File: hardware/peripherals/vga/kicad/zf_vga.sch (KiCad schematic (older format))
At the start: 34 parts, among them J1 Conn_02x04_Odd_Even, J2 Conn_02x13_Odd_Even, J3 DB15_Female, J4 DB9_Male, J5 DB9_Male, SW1 SW_DIP_x03, U1 4040, U10 74HC165, U11 AS6C6264, U12 74HC541, U13 74HC541, U14 74HC541, U2 4040, U3 GAL16V8, U4 GAL16V8, U5 74HC541, U6 74HC541, U7 74HC00, U8 74HC04, U9 74HC74, X1 CXO_DIP14

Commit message: Started PCB
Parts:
- removed J1: Conn_02x04_Odd_Even, symbol Connector_Generic:Conn_02x04_Odd_Even
- C1, C2, C3, C4, C5: footprint (none) -> Capacitor_THT:C_Disc_D7.5mm_W2.5mm_P5.00mm
- J2: footprint (none) -> Connector_IDC:IDC-Header_2x13_P2.54mm_Vertical
- R1, R2, R3, R4, R5, R6, R7, R8: footprint (none) -> Resistor_THT:R_Axial_DIN0207_L6.3mm_D2.5mm_P7.62mm_Horizontal
- SW1: footprint (none) -> Button_Switch_THT:SW_DIP_SPSTx03_Slide_6.7x9.18mm_W7.62mm_P2.54mm_LowProfile
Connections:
- no-connect marks 35 -> 29
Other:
- moved on the sheet: U12

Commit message: Bypass caps
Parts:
- added C10, C11, C12, C13, C14, C15, C16, C17, C18, C19, C20, C6, C7, C8, C9: 0.1uF, Capacitor_THT:C_Disc_D7.5mm_W2.5mm_P5.00mm, symbol Device:C_Small
- SW1: footprint Button_Switch_THT:SW_DIP_SPSTx03_Slide_6.7x9.18mm_W7.62mm_P2.54mm_LowProfile -> Package_DIP:DIP-6_W7.62mm_LongPads
- U1, U10, U2: footprint Package_DIP:DIP-16_W7.62mm -> Package_DIP:DIP-16_W7.62mm_LongPads
- U11: footprint Package_DIP:DIP-28_W15.24mm -> Package_DIP:DIP-28_W15.24mm_LongPads
- U12, U13, U14, U3, U4, U5, U6: footprint Package_DIP:DIP-20_W7.62mm -> Package_DIP:DIP-20_W7.62mm_LongPads
- X1: footprint Oscillator:Oscillator_DIP-14 -> Oscillator:Oscillator_DIP-14_LargePads
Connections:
- net A0: now also U13.11 (Y7), U5.15 (Y3); no longer U13.18 (Y0), U5.18 (Y0)
- net A1: now also U13.12 (Y6), U5.16 (Y2); no longer U13.17 (Y1), U5.17 (Y1)
- net A10: now also U14.18 (Y0), U6.18 (Y0); no longer U14.16 (Y2), U6.12 (Y6)
- net A2: now also U13.13 (Y5), U5.17 (Y1); no longer U13.16 (Y2), U5.16 (Y2)
- net A3: now also U13.14 (Y4), U5.18 (Y0); no longer U13.15 (Y3), U5.15 (Y3)
- net A4: now also U13.15 (Y3), U6.12 (Y6); no longer U13.14 (Y4), U6.18 (Y0)
- net A5: now also U13.16 (Y2), U6.13 (Y5); no longer U13.13 (Y5), U6.17 (Y1)
- net A6: now also U13.17 (Y1), U6.14 (Y4); no longer U13.12 (Y6), U6.16 (Y2)
- net A7: now also U13.18 (Y0); no longer U13.11 (Y7)
- net A8: now also U14.16 (Y2), U6.16 (Y2); no longer U14.18 (Y0), U6.14 (Y4)
- net A9: now also U6.17 (Y1); no longer U6.13 (Y5)
- net D0: now also U12.11 (Y7); no longer U12.18 (Y0)
- net D1: now also U12.12 (Y6); no longer U12.17 (Y1)
- net D2: now also U12.13 (Y5); no longer U12.16 (Y2)
- net D3: now also U12.14 (Y4); no longer U12.15 (Y3)
- net D4: now also U12.15 (Y3); no longer U12.14 (Y4)
- net D5: now also U12.16 (Y2); no longer U12.13 (Y5)
- net D6: now also U12.17 (Y1); no longer U12.12 (Y6)
- net D7: now also U12.18 (Y0); no longer U12.11 (Y7)
- net GND: now also C4.2, C5.2, C10.2, C11.2, C12.2, C13.2, C14.2, C15.2, C16.2, C17.2, C18.2, C19.2, C20.2, C6.2, C7.2, C8.2, C9.2; no longer C4.1, C5.1
- net L0: now also U4.11 (I10/~OE~); no longer U4.1 (I1/CLK)
- net L1: now also U4.9 (I9); no longer U4.2 (I2)
- net L2: now also U4.8 (I8), U6.8 (A6); no longer U4.3 (I3), U6.2 (A0)
- net L3: now also U4.7 (I7), U6.7 (A5); no longer U4.4 (I4), U6.3 (A1)
- net L4: now also U4.6 (I6), U6.6 (A4); no longer U4.5 (I5), U6.4 (A2)
- net L5: now also U4.5 (I5); no longer U4.6 (I6)
- net L6: now also U4.4 (I4), U6.4 (A2); no longer U4.7 (I7), U6.6 (A4)
- net L7: now also U4.3 (I3), U6.3 (A1); no longer U4.8 (I8), U6.7 (A5)
- net L8: now also U4.2 (I2), U6.2 (A0); no longer U4.9 (I9), U6.8 (A6)
- net L9: now also U4.1 (I1/CLK); no longer U4.11 (I10/~OE~)
- net P0: now also U3.11 (I10/~OE~); no longer U3.1 (I1/CLK)
- net P1: now also U3.9 (I9); no longer U3.2 (I2)
- net P2: now also U3.8 (I8); no longer U3.3 (I3)
- net P3: now also U3.7 (I7); no longer U3.4 (I4)
- net P4: now also U3.6 (I6); no longer U3.5 (I5)
- net P5: now also U3.5 (I5), U5.5 (A3); no longer U3.6 (I6), U5.2 (A0)
- net P6: now also U3.4 (I4), U5.4 (A2); no longer U3.7 (I7), U5.3 (A1)
- net P7: now also U3.3 (I3), U5.3 (A1); no longer U3.8 (I8), U5.4 (A2)
- net P8: now also U3.2 (I2), U5.2 (A0); no longer U3.9 (I9), U5.5 (A3)
- net P9: now also U3.1 (I1/CLK); no longer U3.11 (I10/~OE~)
- net PA0: now also U12.9 (A7); no longer U12.2 (A0)
- net PA1: now also U12.8 (A6); no longer U12.3 (A1)
- net PA2: now also U12.7 (A5); no longer U12.4 (A2)
- net PA3: now also U12.6 (A4); no longer U12.5 (A3)
- net PA4: now also U12.5 (A3); no longer U12.6 (A4)
- net PA5: now also U12.4 (A2); no longer U12.7 (A5)
- net PA6: now also U12.3 (A1); no longer U12.8 (A6)
- net PA7: now also U12.2 (A0); no longer U12.9 (A7)
- net PB0: now also U13.9 (A7); no longer U13.2 (A0)
- net PB1: now also U13.8 (A6); no longer U13.3 (A1)
- net PB2: now also U13.7 (A5); no longer U13.4 (A2)
- net PB3: now also U13.6 (A4); no longer U13.5 (A3)
- net PB4: now also U13.5 (A3); no longer U13.6 (A4)
- net PB5: now also U13.4 (A2); no longer U13.7 (A5)
- net PB6: now also U13.3 (A1); no longer U13.8 (A6)
- net PB7: now also U13.2 (A0); no longer U13.9 (A7)
- net PC0: now also U14.4 (A2); no longer U14.2 (A0)
- net PC2: now also U14.2 (A0); no longer U14.4 (A2)
- net VCC: now also C10.1, C11.1, C12.1, C13.1, C14.1, C15.1, C16.1, C17.1, C18.1, C19.1, C20.1, C6.1, C7.1, C8.1, C9.1
- net VIDOUT: now reaches SW1.1, SW1.2, SW1.3, U10.9 (Q7)
- net at J3.13 (P13), R7.2: now also C4.1
- net at J3.14 (P14), R8.2: now also C5.1; no longer C4.2, C5.2
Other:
- moved on the sheet: C4, C5, J3, R4, R5, R6, R7, R8, SW1

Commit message: Expansion port footprint
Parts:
- J2: value Conn_02x13_Odd_Even -> Z-FIGHTER Expansion Port; footprint Connector_IDC:IDC-Header_2x13_P2.54mm_Vertical -> Z-FIGHTER:Z-FIGHTER_Expansion_Port; symbol Connector_Generic:Conn_02x13_Odd_Even -> Connector_Generic:Conn_02x17_Odd_Even
- U7, U8, U9: footprint Package_DIP:DIP-14_W7.62mm -> Package_DIP:DIP-14_W7.62mm_LongPads
- U8: footprint (none) -> Package_DIP:DIP-14_W7.62mm_LongPads
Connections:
- net GND: now also J2.27 (Pin_27)
- net VCC: now also J2.28 (Pin_28)
- no-connect marks 29 -> 35
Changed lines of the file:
@@
 F 0 "U9" H 4900 7481 50  0001 C CNN
 F 1 "74HC74" H 4900 7389 50  0001 C CNN
-F 2 "Package_DIP:DIP-14_W7.62mm" H 4900 7000 50  0001 C CNN
+F 2 "Package_DIP:DIP-14_W7.62mm_LongPads" H 4900 7000 50  0001 C CNN
 F 3 "74xx/74hc_hct74.pdf" H 4900 7000 50  0001 C CNN
 	2    4900 7000
@@
 F 0 "U9" V 4625 7600 50  0001 C CNN
 F 1 "74HC74" V 4624 7600 50  0001 C CNN
-F 2 "Package_DIP:DIP-14_W7.62mm" H 4900 7600 50  0001 C CNN
+F 2 "Package_DIP:DIP-14_W7.62mm_LongPads" H 4900 7600 50  0001 C CNN
 F 3 "74xx/74hc_hct74.pdf" H 4900 7600 50  0001 C CNN
 	3    4900 7600
@@
 F 0 "U9" H 4900 6781 50  0000 C CNN
 F 1 "74HC74" H 4900 6690 50  0000 C CNN
-F 2 "Package_DIP:DIP-14_W7.62mm" H 4900 6300 50  0001 C CNN
+F 2 "Package_DIP:DIP-14_W7.62mm_LongPads" H 4900 6300 50  0001 C CNN
 F 3 "74xx/74hc_hct74.pdf" H 4900 6300 50  0001 C CNN
 	1    4900 6300
@@
 	1    0    0    -1
 $EndComp
+Text GLabel 10200 2100 0    50   Input ~ 0
+PC6
+Text GLabel 10200 2000 0    50   Input ~ 0
+PC5
+Text GLabel 10200 1500 0    50   Input ~ 0
+PC0
+Text GLabel 10200 1600 0    50   Input ~ 0
+PC1
+Text GLabel 10200 1700 0    50   Input ~ 0
+PC2
+Text GLabel 10700 2300 2    50   Input ~ 0
+PB0
 Text GLabel 10700 2400 2    50   Input ~ 0
-PC6
+PB1
 Text GLabel 10700 2500 2    50   Input ~ 0
-PC5
-NoConn ~ 10700 2300
-Text GLabel 10700 3000 2    50   Input ~ 0
-PC0
-Text GLabel 10700 2900 2    50   Input ~ 0
-PC1
-Text GLabel 10700 2800 2    50   Input ~ 0
-PC2
-Text GLabel 10200 2200 0    50   Input ~ 0
-PB0
-Text GLabel 10200 2100 0    50   Input ~ 0
-PB1
-Text GLabel 10200 2000 0    50   Input ~ 0
 PB2
-Text GLabel 10200 1900 0    50   Input ~ 0
+Text GLabel 10700 2600 2    50   Input ~ 0
 PB3
 $Comp
 L power:GND #PWR0114
 U 1 1 622D7A61
-P 9850 1850
-F 0 "#PWR0114" H 9850 1600 50  0001 C CNN
-F 1 "GND" H 9855 1677 50  0000 C CNN
-F 2 "" H 9850 1850 50  0001 C CNN
-F 3 "" H 9850 1850 50  0001 C CNN
-	1    9850 1850
-	1    0    0    -1
-$EndComp
-NoConn ~ 10700 2700
-Text GLabel 10700 2600 2    50   Input ~ 0
+P 11050 2700
+F 0 "#PWR0114" H 11050 2450 50  0001 C CNN
+F 1 "GND" H 11055 2527 50  0000 C CNN
+F 2 "" H 11050 2700 50  0001 C CNN
+F 3 "" H 11050 2700 50  0001 C CNN
+	1    11050 2700
+	1    0    0    -1
+$EndComp
+Text GLabel 10200 1900 0    50   Input ~ 0
 DATARDY
 Text GLabel 10950 3950 2    50   Input ~ 0
@@
 Text GLabel 8300 4050 0    50   Input ~ 0
 PB4
+Text GLabel 10200 2600 0    50   Input ~ 0
+PB4
+Text GLabel 10200 2500 0    50   Input ~ 0
+PB5
+Text GLabel 10200 2400 0    50   Input ~ 0
+PB6
+Text GLabel 10200 2300 0    50   Input ~ 0
+PB7
+Text GLabel 10700 2200 2    50   Input ~ 0
+PA7
+Text GLabel 10700 2100 2    50   Input ~ 0
+PA6
+Text GLabel 10700 2000 2    50   Input ~ 0
+PA5
 Text GLabel 10700 1900 2    50   Input ~ 0
-PB4
-Text GLabel 10700 2000 2    50   Input ~ 0
-PB5
-Text GLabel 10700 2100 2    50   Input ~ 0
-PB6
-Text GLabel 10700 2200 2    50   Input ~ 0
-PB7
-Text GLabel 10200 2300 0    50   Input ~ 0
-PA7
-Text GLabel 10200 2400 0    50   Input ~ 0
-PA6
-Text GLabel 10200 2500 0    50   Input ~ 0
-PA5
-Text GLabel 10200 2600 0    50   Input ~ 0
 PA4
-Text GLabel 10200 2700 0    50   Input ~ 0
+Text GLabel 10700 1800 2    50   Input ~ 0
 PA3
-Text GLabel 10200 2800 0    50   Input ~ 0
+Text GLabel 10700 1700 2    50   Input ~ 0
 PA2
-Text GLabel 10200 2900 0    50   Input ~ 0
+Text GLabel 10700 1600 2    50   Input ~ 0
 PA1
-Text GLabel 10200 3000 0    50   Input ~ 0
+Text GLabel 10700 1500 2    50   Input ~ 0
 PA0
 $Comp
@@
 Text Notes 10050 3150 0    50   ~ 0
 Z-Fighter Connectors
-$Comp
-L Connector_Generic:Conn_02x13_Odd_Even J2
-U 1 1 621FEB7B
-P 10400 2400
-F 0 "J2" H 10450 3217 50  0000 C CNN
-F 1 "Conn_02x13_Odd_Even" H 10450 3126 50  0000 C CNN
-F 2 "Connector_IDC:IDC-Header_2x13_P2.54mm_Vertical" H 10400 2400 50  0001 C CNN
-F 3 "~" H 10400 2400 50  0001 C CNN
-	1    10400 2400
-	1    0    0    -1
-$EndComp
 $Comp
 L power:GND #PWR0134
@@
 L9
 Wire Wire Line
-	9850 1800 10200 1800
+	11050 2700 10700 2700
 $Comp
 L 74xx:74HC04 U8
@@
 F 0 "U8" H 4900 1367 50  0000 C CNN
 F 1 "74HC04" H 4900 1276 50  0000 C CNN
-F 2 "Package_DIP:DIP-14_W7.62mm" H 4900 1050 50  0001 C CNN
+F 2 "Package_DIP:DIP-14_W7.62mm_LongPads" H 4900 1050 50  0001 C CNN
 F 3 "https://assets.nexperia.com/documents/data-sheet/74HC_HCT04.pdf" H 4900 1050 50  0001 C CNN
 	1    4900 1050
@@
 F 0 "U8" H 4900 3025 50  0001 C CNN
 F 1 "74HC04" H 4900 3026 50  0001 C CNN
-F 2 "" H 4900 2800 50  0001 C CNN
+F 2 "Package_DIP:DIP-14_W7.62mm_LongPads" H 4900 2800 50  0001 C CNN
 F 3 "https://assets.nexperia.com/documents/data-sheet/74HC_HCT04.pdf" H 4900 2800 50  0001 C CNN
 	6    4900 2800
@@
 F 0 "U8" H 4900 2767 50  0001 C CNN
 F 1 "74HC04" H 4900 2676 50  0001 C CNN
-F 2 "" H 4900 2450 50  0001 C CNN
+F 2 "Package_DIP:DIP-14_W7.62mm_LongPads" H 4900 2450 50  0001 C CNN
 F 3 "https://assets.nexperia.com/documents/data-sheet/74HC_HCT04.pdf" H 4900 2450 50  0001 C CNN
 	5    4900 2450
@@
 F 0 "U8" H 4900 2417 50  0001 C CNN
 F 1 "74HC04" H 4900 2326 50  0001 C CNN
-F 2 "" H 4900 2100 50  0001 C CNN
+F 2 "Package_DIP:DIP-14_W7.62mm_LongPads" H 4900 2100 50  0001 C CNN
 F 3 "https://assets.nexperia.com/documents/data-sheet/74HC_HCT04.pdf" H 4900 2100 50  0001 C CNN
 	4    4900 2100
@@
 F 0 "U8" H 4900 2067 50  0001 C CNN
 F 1 "74HC04" H 4900 1976 50  0001 C CNN
-F 2 "" H 4900 1750 50  0001 C CNN
+F 2 "Package_DIP:DIP-14_W7.62mm_LongPads" H 4900 1750 50  0001 C CNN
 F 3 "https://assets.nexperia.com/documents/data-sheet/74HC_HCT04.pdf" H 4900 1750 50  0001 C CNN
 	3    4900 1750
@@
 F 0 "U8" H 4900 1717 50  0001 C CNN
 F 1 "74HC04" H 4900 1626 50  0001 C CNN
-F 2 "" H 4900 1400 50  0001 C CNN
+F 2 "Package_DIP:DIP-14_W7.62mm_LongPads" H 4900 1400 50  0001 C CNN
 F 3 "https://assets.nexperia.com/documents/data-sheet/74HC_HCT04.pdf" H 4900 1400 50  0001 C CNN
 	2    4900 1400
@@
 F 0 "U8" V 4625 3200 50  0001 C CNN
 F 1 "74HC04" V 4624 3200 50  0001 C CNN
-F 2 "" H 4900 3200 50  0001 C CNN
+F 2 "Package_DIP:DIP-14_W7.62mm_LongPads" H 4900 3200 50  0001 C CNN
 F 3 "https://assets.nexperia.com/documents/data-sheet/74HC_HCT04.pdf" H 4900 3200 50  0001 C CNN
 	7    4900 3200
@@
 F 0 "U7" H 4900 4275 50  0000 C CNN
 F 1 "74HC00" H 4900 4184 50  0000 C CNN
-F 2 "Package_DIP:DIP-14_W7.62mm" H 4900 3950 50  0001 C CNN
+F 2 "Package_DIP:DIP-14_W7.62mm_LongPads" H 4900 3950 50  0001 C CNN
 F 3 "http://www.ti.com/lit/gpn/sn74hc00" H 4900 3950 50  0001 C CNN
 	1    4900 3950
@@
 F 0 "U7" H 4900 4533 50  0001 C CNN
 F 1 "74HC00" H 4900 4534 50  0001 C CNN
-F 2 "Package_DIP:DIP-14_W7.62mm" H 4900 4300 50  0001 C CNN
+F 2 "Package_DIP:DIP-14_W7.62mm_LongPads" H 4900 4300 50  0001 C CNN
 F 3 "http://www.ti.com/lit/gpn/sn74hc00" H 4900 4300 50  0001 C CNN
 	2    4900 4300
@@
 F 0 "U7" V 4625 5400 50  0001 C CNN
 F 1 "74HC00" V 4624 5400 50  0001 C CNN
-F 2 "Package_DIP:DIP-14_W7.62mm" H 4900 5400 50  0001 C CNN
+F 2 "Package_DIP:DIP-14_W7.62mm_LongPads" H 4900 5400 50  0001 C CNN
 F 3 "http://www.ti.com/lit/gpn/sn74hc00" H 4900 5400 50  0001 C CNN
 	5    4900 5400
@@
 F 0 "U7" H 4900 4975 50  0001 C CNN
 F 1 "74HC00" H 4900 4883 50  0001 C CNN
-F 2 "Package_DIP:DIP-14_W7.62mm" H 4900 4650 50  0001 C CNN
+F 2 "Package_DIP:DIP-14_W7.62mm_LongPads" H 4900 4650 50  0001 C CNN
 F 3 "http://www.ti.com/lit/gpn/sn74hc00" H 4900 4650 50  0001 C CNN
 	3    4900 4650
@@
 F 0 "U7" H 4900 5325 50  0001 C CNN
 F 1 "74HC00" H 4900 5233 50  0001 C CNN
-F 2 "Package_DIP:DIP-14_W7.62mm" H 4900 5000 50  0001 C CNN
+F 2 "Package_DIP:DIP-14_W7.62mm_LongPads" H 4900 5000 50  0001 C CNN
 F 3 "http://www.ti.com/lit/gpn/sn74hc00" H 4900 5000 50  0001 C CNN
 	4    4900 5000
@@
 Wire Wire Line
 	3350 5150 3350 5200
-Wire Wire Line
-	9850 1800 9850 1850
 Wire Wire Line
 	1700 5150 1700 5200
@@
 L power:VCC #PWR0112
 U 1 1 622CC803
-P 11000 1800
-F 0 "#PWR0112" H 11000 1650 50  0001 C CNN
-F 1 "VCC" H 11015 1973 50  0000 C CNN
-F 2 "" H 11000 1800 50  0001 C CNN
-F 3 "" H 11000 1800 50  0001 C CNN
-	1    11000 1800
-	1    0    0    -1
-$EndComp
-Wire Wire Line
-	11000 1800 10700 1800
+P 9750 1400
+F 0 "#PWR0112" H 9750 1250 50  0001 C CNN
+F 1 "VCC" H 9765 1573 50  0000 C CNN
+F 2 "" H 9750 1400 50  0001 C CNN
+F 3 "" H 9750 1400 50  0001 C CNN
+	1    9750 1400
+	1    0    0    -1
+$EndComp
 Connection ~ 10450 5050
 Connection ~ 8800 5050
@@
 	1    0    0    -1
 $EndComp
+$Comp
+L Connector_Generic:Conn_02x17_Odd_Even J2
+U 1 1 621FEB7B
+P 10500 1900
+F 0 "J2" H 10550 2835 50  0000 C CNN
+F 1 "Z-FIGHTER Expansion Port" H 10550 2626 50  0001 C CNN
+F 2 "Z-FIGHTER:Z-FIGHTER_Expansion_Port" H 10500 1900 50  0001 C CNN
+F 3 "~" H 10500 1900 50  0001 C CNN
+	1    10500 1900
+	-1   0    0    1
+$EndComp
+Wire Wire Line
+	11050 2700 11050 1400
+Wire Wire Line
+	11050 1400 10700 1400
+Connection ~ 11050 2700
+Wire Wire Line
+	9750 1400 9750 2700
+Connection ~ 9750 1400
+Wire Wire Line
+	9750 1400 10200 1400
+Wire Wire Line
+	9750 2700 10200 2700
+NoConn ~ 10200 1100
+NoConn ~ 10200 1200
+NoConn ~ 10200 1300
+NoConn ~ 10700 1300
+NoConn ~ 10700 1200
+NoConn ~ 10700 1100
+NoConn ~ 10200 2200
+NoConn ~ 10200 1800
 $EndSCHEMATC

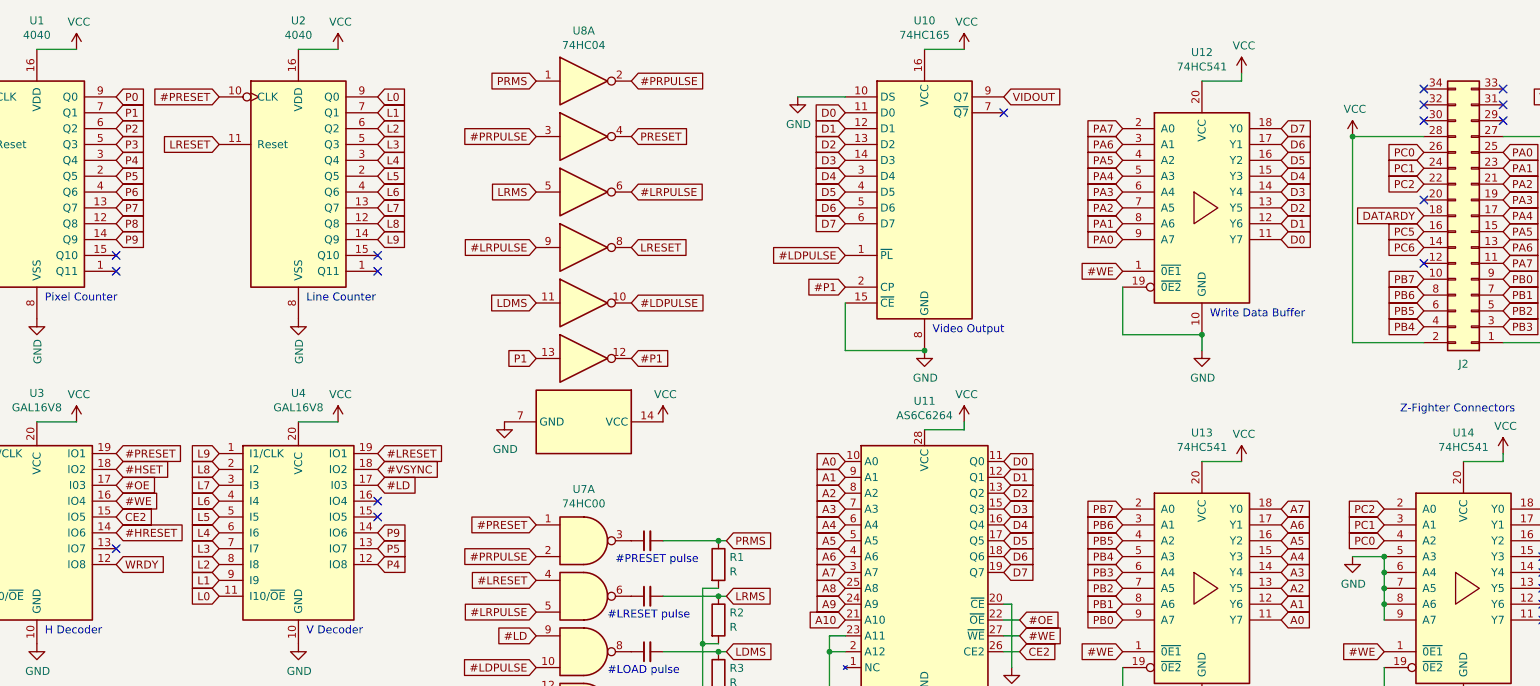
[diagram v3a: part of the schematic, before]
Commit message: Connected #RESET from ZF
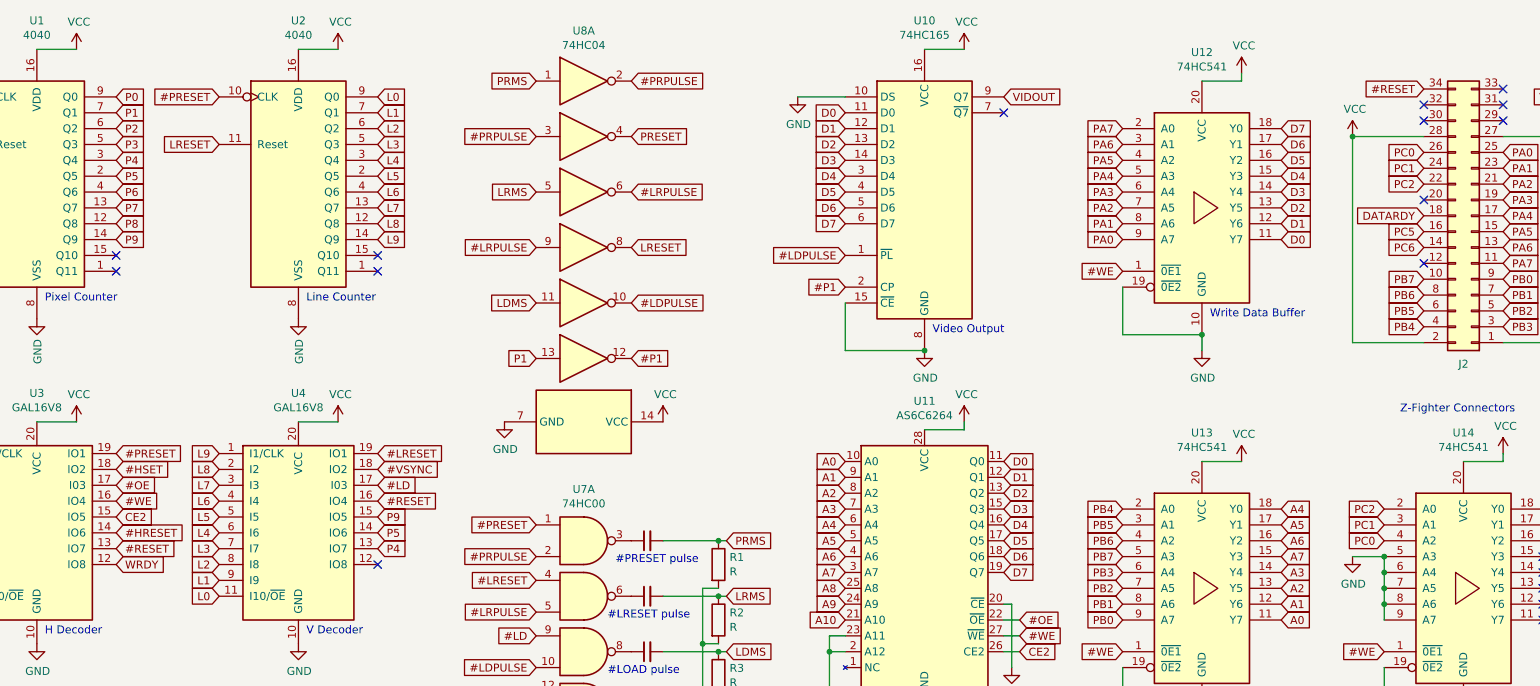
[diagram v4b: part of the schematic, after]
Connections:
- net A4: now also U13.18 (Y0); no longer U13.15 (Y3)
- net A5: now also U13.17 (Y1); no longer U13.16 (Y2)
- net A6: now also U13.16 (Y2); no longer U13.17 (Y1)
- net A7: now also U13.15 (Y3); no longer U13.18 (Y0)
- net P4: now also U4.13 (IO7); no longer U4.12 (IO8)
- net P5: now also U4.14 (IO6); no longer U4.13 (IO7)
- net P9: now also U4.15 (IO5); no longer U4.14 (IO6)
- net PB4: now also U13.2 (A0); no longer U13.5 (A3)
- net PB5: now also U13.3 (A1); no longer U13.4 (A2)
- net PB6: now also U13.4 (A2); no longer U13.3 (A1)
- net PB7: now also U13.5 (A3); no longer U13.2 (A0)
- net #RESET: now reaches U3.13 (IO7)
- net #RESET: now also J2.34 (Pin_34), U4.16 (IO4)
- no-connect marks 35 -> 32
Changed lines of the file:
@@
 Text GLabel 8300 4150 0    50   Input ~ 0
 PB3
-Text GLabel 8300 3750 0    50   Input ~ 0
-PB7
-Text GLabel 8300 3850 0    50   Input ~ 0
-PB6
-Text GLabel 8300 3950 0    50   Input ~ 0
-PB5
-Text GLabel 8300 4050 0    50   Input ~ 0
-PB4
 Text GLabel 10200 2600 0    50   Input ~ 0
 PB4
@@
 Text GLabel 850  6400 0    50   Input ~ 0
 #OE
-NoConn ~ 1950 4000
 Text GLabel 1950 3900 2    50   Input ~ 0
 #HRESET
-NoConn ~ 3600 3700
-NoConn ~ 3600 3800
+Text GLabel 3600 3900 2    50   Input ~ 0
+P5
 Text GLabel 3600 4000 2    50   Input ~ 0
-P5
-Text GLabel 3600 4100 2    50   Input ~ 0
 P4
 Text GLabel 950  3600 0    50   Input ~ 0
@@
 Text GLabel 1950 3400 2    50   Input ~ 0
 #PRESET
-Text GLabel 1950 4100 2    50   Input ~ 0
-WRDY
 Text GLabel 1950 3500 2    50   Input ~ 0
 #HSET
@@
 Text GLabel 1950 3800 2    50   Input ~ 0
 CE2
-Text GLabel 3600 3900 2    50   Input ~ 0
+Text GLabel 3600 3800 2    50   Input ~ 0
 P9
 $Comp
@@
 Text GLabel 3600 3500 2    50   Input ~ 0
 #VSYNC
-$Comp
-L Logic_Programmable:GAL16V8 U3
-U 1 1 62173FE1
-P 1450 3900
-F 0 "U3" H 1450 4781 50  0000 C CNN
-F 1 "GAL16V8" H 1450 4690 50  0000 C CNN
-F 2 "Package_DIP:DIP-20_W7.62mm_LongPads" H 1450 3900 50  0001 C CNN
-F 3 "" H 1450 3900 50  0001 C CNN
-	1    1450 3900
-	1    0    0    -1
-$EndComp
 Wire Wire Line
 	950  6400 850  6400
@@
 Text GLabel 9300 4150 2    50   Input ~ 0
 A3
-Text GLabel 9300 4050 2    50   Input ~ 0
-A4
-Text GLabel 9300 3950 2    50   Input ~ 0
-A5
-Text GLabel 9300 3850 2    50   Input ~ 0
-A6
-Text GLabel 9300 3750 2    50   Input ~ 0
-A7
 Text GLabel 9300 4250 2    50   Input ~ 0
 A2
@@
 Wire Wire Line
 	9750 2700 10200 2700
-NoConn ~ 10200 1100
 NoConn ~ 10200 1200
 NoConn ~ 10200 1300
@@
 NoConn ~ 10200 2200
 NoConn ~ 10200 1800
+$Comp
+L Logic_Programmable:GAL16V8 U3
+U 1 1 62173FE1
+P 1450 3900
+F 0 "U3" H 1450 4781 50  0000 C CNN
+F 1 "GAL16V8" H 1450 4690 50  0000 C CNN
+F 2 "Package_DIP:DIP-20_W7.62mm_LongPads" H 1450 3900 50  0001 C CNN
+F 3 "" H 1450 3900 50  0001 C CNN
+	1    1450 3900
+	1    0    0    -1
+$EndComp
+Text GLabel 1950 4100 2    50   Input ~ 0
+WRDY
+Text GLabel 8300 4050 0    50   Input ~ 0
+PB7
+Text GLabel 8300 3950 0    50   Input ~ 0
+PB6
+Text GLabel 8300 3850 0    50   Input ~ 0
+PB5
+Text GLabel 8300 3750 0    50   Input ~ 0
+PB4
+Text GLabel 9300 3750 2    50   Input ~ 0
+A4
+Text GLabel 9300 3850 2    50   Input ~ 0
+A5
+Text GLabel 9300 3950 2    50   Input ~ 0
+A6
+Text GLabel 9300 4050 2    50   Input ~ 0
+A7
+Text GLabel 10200 1100 0    50   Input ~ 0
+#RESET
+Text GLabel 1950 4000 2    50   Input ~ 0
+#RESET
+Text GLabel 3600 3700 2    50   Input ~ 0
+#RESET
+NoConn ~ 3600 4100
 $EndSCHEMATC
